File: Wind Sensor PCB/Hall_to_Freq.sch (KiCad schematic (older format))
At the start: 13 parts

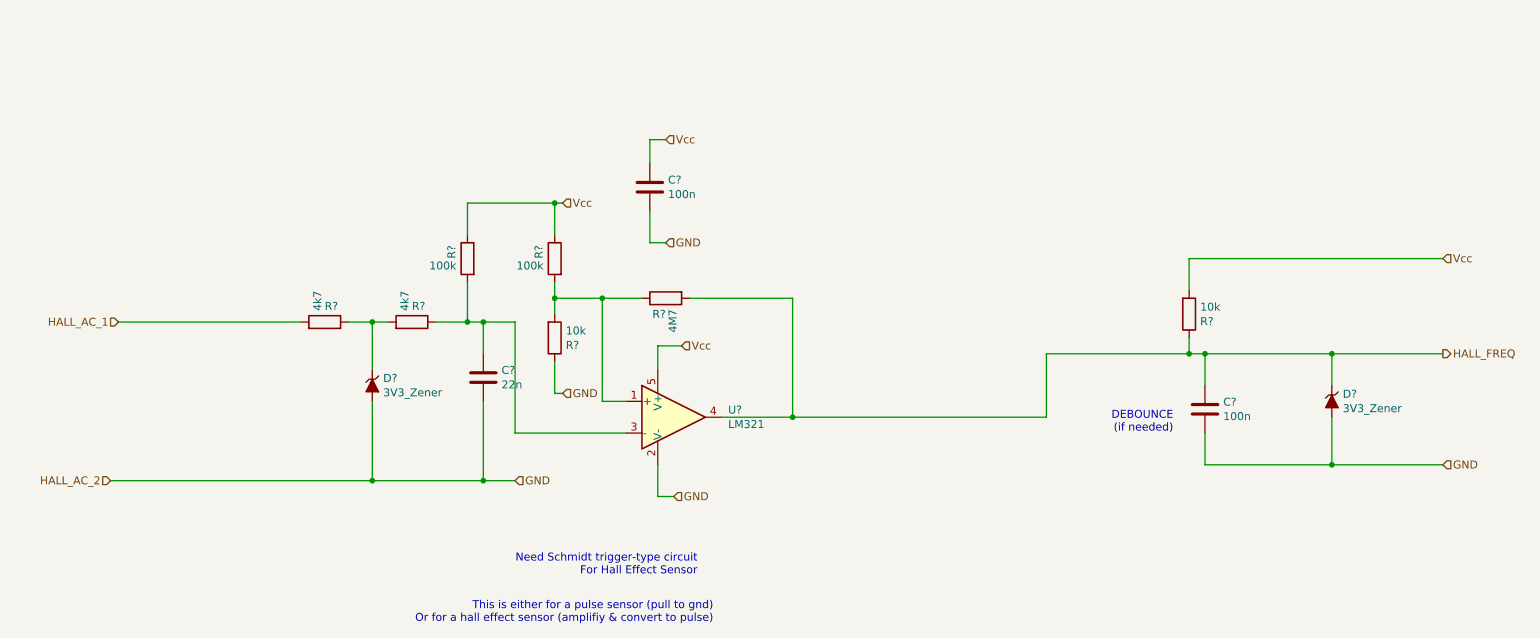
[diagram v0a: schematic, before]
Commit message: Updated PCB
Version 1 of the PCB with ATMEGA328 used...
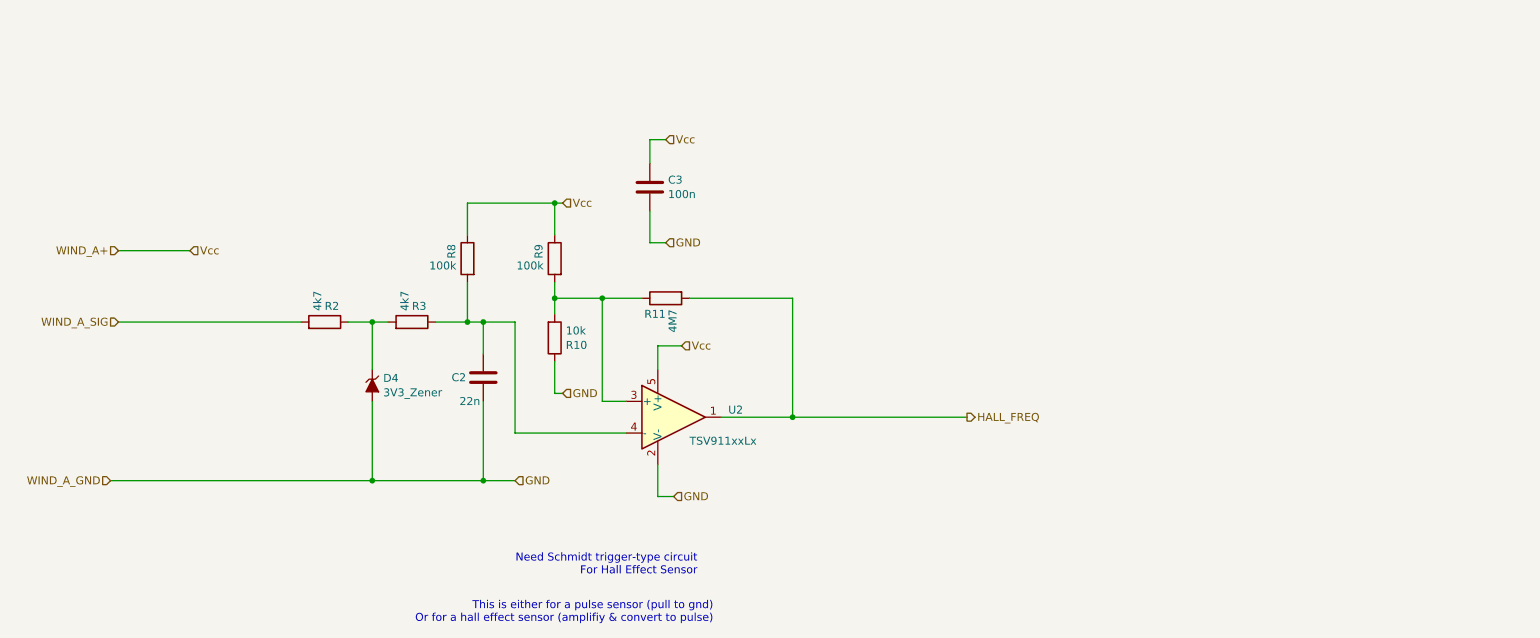
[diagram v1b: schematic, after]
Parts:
- removed C?: 100n, symbol device:C
- removed D?: 3V3_Zener, symbol matts_components:ZENERsmall
- removed R26: 10k, REInnovationFootprint:SM0805, symbol Device:R
- removed U?: LM321, REInnovationFootprint:SM_SOT-23-5, symbol Amplifier_Operational:LM321
- added U2: TSV911xxLx, REInnovationFootprint:SM_SOT-23-5, symbol Amplifier_Operational:TSV911xxLx
- C2, C3: renamed from C?; footprint (none) -> REInnovationFootprint:SM_C_0805
- D4: renamed from D?; footprint (none) -> REInnovationFootprint:SOT23
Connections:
- net GND: now also U2.2 (V-)
- net HALL_FREQ: now also U2.1
- net Vcc: now also U2.5 (V+)
- net at C2.1, R25.1, R35.2: now also U2.4 (-)
- net at R36.2, R37.2, R38.1: now also U2.3 (+)
- net HALL_AC_1 renamed WIND_A_SIG
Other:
- note removed: "DEBOUNCE\n(if needed)\n"
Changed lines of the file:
@@
 $Descr A4 11693 8268
 encoding utf-8
-Sheet 6 6
+Sheet 4 4
 Title ""
 Date ""
@@
 Comment4 ""
 $EndDescr
-Wire Wire Line
-	8300 3500 8300 3600
-Text Notes 8200 4100 2    50   ~ 0
-DEBOUNCE\n(if needed)\n
-Wire Wire Line
-	9200 3800 9200 3600
-Connection ~ 9200 3600
-Wire Wire Line
-	9200 3600 8400 3600
-$Comp
-L Device:R R?
-U 1 1 60751298
-P 8300 3350
-AR Path="/60751298" Ref="R?"  Part="1"
-AR Path="/6073E175/60751298" Ref="R26"  Part="1"
-AR Path="/60F57495/60751298" Ref="R?"  Part="1"
-F 0 "R?" H 8370 3396 50  0000 L CNN
-F 1 "10k" H 8370 3305 50  0000 L CNN
-F 2 "REInnovationFootprint:SM0805" V 8230 3350 50  0001 C CNN
-F 3 "~" H 8300 3350 50  0001 C CNN
-F 4 "Farnell" H 8300 3350 50  0001 C CNN "Supplier 1"
-F 5 "2073607" H 8300 3350 50  0001 C CNN "Supplier 1 Code"
-F 6 "https://uk.farnell.com/multicomp/mcmr08x1002ftl/res-10k-1-0-125w-0805-ceramic/dp/2073607?st=0805%20resistor%2010k" H 8300 3350 50  0001 C CNN "Supplier 1 Web"
-F 7 "0.02" H 8300 3350 50  0001 C CNN "Supplier 1 Cost"
-F 8 "MCMR08X1002FTL" H 8300 3350 50  0001 C CNN "Manufacturer Part"
-F 9 "C17414" H 8300 3350 50  0001 C CNN "LCSC"
-F 10 "Y" H 8300 3350 50  0001 C CNN "JLCPCB Add"
-F 11 "0.0029" H 8300 3350 50  0001 C CNN "JLCPCB Cost"
-	1    8300 3350
-	1    0    0    1
-$EndComp
-Wire Wire Line
-	9200 4300 8400 4300
-Text HLabel 9900 3000 2    50   Input ~ 0
-Vcc
-Text HLabel 9900 3600 2    50   Output ~ 0
+Text HLabel 6900 4000 2    50   Output ~ 0
 HALL_FREQ
-Text HLabel 9900 4300 2    50   Input ~ 0
-GND
-Text HLabel 1550 3400 0    50   Input ~ 0
-HALL_AC_1
-Text HLabel 1500 4400 0    50   Input ~ 0
-HALL_AC_2
 Text Notes 5200 5000 2    50   ~ 0
 Need Schmidt trigger-type circuit\nFor Hall Effect Sensor\n
-Wire Wire Line
-	9200 3600 9900 3600
-Wire Wire Line
-	8300 3000 9900 3000
-Wire Wire Line
-	8300 3000 8300 3200
-Wire Wire Line
-	9900 4300 9200 4300
-Connection ~ 9200 4300
-Wire Wire Line
-	8400 3600 8400 3800
-Connection ~ 8400 3600
-Wire Wire Line
-	8400 3600 8300 3600
-$Comp
-L Amplifier_Operational:LM321 U?
-U 1 1 609A25E3
-P 5050 4000
-F 0 "U?" H 5394 4046 50  0000 L CNN
-F 1 "LM321" H 5394 3955 50  0000 L CNN
-F 2 "REInnovationFootprint:SM_SOT-23-5" H 5050 4000 50  0001 C CNN
-F 3 "http://www.ti.com/lit/ds/symlink/lm321.pdf" H 5050 4000 50  0001 C CNN
-F 4 "Unisonic Tech" H 5050 4000 50  0001 C CNN "Manufacturer"
-F 5 "LM321G-AE5-R" H 5050 4000 50  0001 C CNN "Manufacturer Part"
-F 6 "C100068" H 5050 4000 50  0001 C CNN "LCSC"
-F 7 "Y" H 5050 4000 50  0001 C CNN "JLCPCB Add"
-F 8 "0.0778" H 5050 4000 50  0001 C CNN "JLCPCB Cost"
-	1    5050 4000
-	1    0    0    -1
-$EndComp
 Text HLabel 5100 3550 2    50   Input ~ 0
 Vcc
@@
 AR Path="/607446F0" Ref="R?"  Part="1"
 AR Path="/6073E175/607446F0" Ref="R25"  Part="1"
-AR Path="/60F57495/607446F0" Ref="R?"  Part="1"
-F 0 "R?" V 3500 3400 50  0000 L CNN
+AR Path="/60F57495/607446F0" Ref="R3"  Part="1"
+F 0 "R3" V 3500 3400 50  0000 L CNN
 F 1 "4k7" H 3470 3355 50  0000 L CNN
 F 2 "REInnovationFootprint:SM0805" V 3330 3400 50  0001 C CNN
@@
 AR Path="/607455DE" Ref="R?"  Part="1"
 AR Path="/6073E175/607455DE" Ref="R36"  Part="1"
-AR Path="/60F57495/607455DE" Ref="R?"  Part="1"
-F 0 "R?" V 4400 3000 50  0000 L CNN
+AR Path="/60F57495/607455DE" Ref="R9"  Part="1"
+F 0 "R9" V 4400 3000 50  0000 L CNN
 F 1 "100k" H 4370 2955 50  0000 L CNN
 F 2 "REInnovationFootprint:SM0805" V 4230 3000 50  0001 C CNN
@@
 AR Path="/60748ED5" Ref="R?"  Part="1"
 AR Path="/6073E175/60748ED5" Ref="R38"  Part="1"
-AR Path="/60F57495/60748ED5" Ref="R?"  Part="1"
-F 0 "R?" V 5100 3250 50  0000 L CNN
+AR Path="/60F57495/60748ED5" Ref="R11"  Part="1"
+F 0 "R11" V 5100 3250 50  0000 L CNN
 F 1 "4M7" H 5070 3205 50  0000 L CNN
 F 2 "REInnovationFootprint:SM0805" V 4930 3250 50  0001 C CNN
@@
 Wire Wire Line
 	5800 3250 5800 4000
-Connection ~ 5800 4000
-Wire Wire Line
-	5800 4000 7400 4000
 Wire Wire Line
 	4300 3150 4300 3250
@@
 Wire Wire Line
 	3750 3400 3850 3400
-Wire Wire Line
-	8300 3600 7400 3600
-Wire Wire Line
-	7400 3600 7400 4000
-Connection ~ 8300 3600
 Wire Wire Line
 	4050 4400 3850 4400
@@
 AR Path="/6079CF2E" Ref="R?"  Part="1"
 AR Path="/6073E175/6079CF2E" Ref="R37"  Part="1"
-AR Path="/60F57495/6079CF2E" Ref="R?"  Part="1"
-F 0 "R?" H 4370 3546 50  0000 L CNN
+AR Path="/60F57495/6079CF2E" Ref="R10"  Part="1"
+F 0 "R10" H 4370 3546 50  0000 L CNN
 F 1 "10k" H 4370 3455 50  0000 L CNN
 F 2 "REInnovationFootprint:SM0805" V 4230 3500 50  0001 C CNN
@@
 AR Path="/6079D863" Ref="R?"  Part="1"
 AR Path="/6073E175/6079D863" Ref="R35"  Part="1"
-AR Path="/60F57495/6079D863" Ref="R?"  Part="1"
-F 0 "R?" V 3850 3000 50  0000 L CNN
+AR Path="/60F57495/6079D863" Ref="R8"  Part="1"
+F 0 "R8" V 3850 3000 50  0000 L CNN
 F 1 "100k" H 3820 2955 50  0000 L CNN
 F 2 "REInnovationFootprint:SM0805" V 3680 3000 50  0001 C CNN
@@
 AR Path="/6079E09B" Ref="R?"  Part="1"
 AR Path="/6073E175/6079E09B" Ref="R24"  Part="1"
-AR Path="/60F57495/6079E09B" Ref="R?"  Part="1"
-F 0 "R?" V 2950 3400 50  0000 L CNN
+AR Path="/60F57495/6079E09B" Ref="R2"  Part="1"
+F 0 "R2" V 2950 3400 50  0000 L CNN
 F 1 "4k7" H 2920 3355 50  0000 L CNN
 F 2 "REInnovationFootprint:SM0805" V 2780 3400 50  0001 C CNN
@@
 $EndComp
 Wire Wire Line
-	1550 3400 2700 3400
-Wire Wire Line
 	1500 4400 3150 4400
 $Comp
-L matts_components:ZENERsmall D?
-U 1 1 60F5F219
-P 9200 3900
-F 0 "D?" V 9154 3969 50  0000 L CNN
-F 1 "3V3_Zener" V 9245 3969 50  0000 L CNN
-F 2 "" H 9200 3900 50  0000 C CNN
-F 3 "" H 9200 3900 50  0000 C CNN
-	1    9200 3900
-	0    1    1    0
-$EndComp
-$Comp
-L matts_components:ZENERsmall D?
+L matts_components:ZENERsmall D4
 U 1 1 60F5F616
 P 3150 3800
-F 0 "D?" V 3104 3869 50  0000 L CNN
+F 0 "D4" V 3104 3869 50  0000 L CNN
 F 1 "3V3_Zener" V 3195 3869 50  0000 L CNN
-F 2 "" H 3150 3800 50  0000 C CNN
+F 2 "REInnovationFootprint:SOT23" H 3150 3800 50  0001 C CNN
 F 3 "" H 3150 3800 50  0000 C CNN
 	1    3150 3800
@@
 $EndComp
 $Comp
-L device:C C?
-U 1 1 60F5FBE8
-P 8400 3950
-F 0 "C?" H 8515 3996 50  0000 L CNN
-F 1 "100n" H 8515 3905 50  0000 L CNN
-F 2 "" H 8438 3800 50  0001 C CNN
-F 3 "~" H 8400 3950 50  0001 C CNN
-	1    8400 3950
-	1    0    0    -1
-$EndComp
-$Comp
-L device:C C?
+L device:C C3
 U 1 1 60F5FEAC
 P 4900 2550
-F 0 "C?" H 5015 2596 50  0000 L CNN
+F 0 "C3" H 5015 2596 50  0000 L CNN
 F 1 "100n" H 5015 2505 50  0000 L CNN
-F 2 "" H 4938 2400 50  0001 C CNN
+F 2 "REInnovationFootprint:SM_C_0805" H 4938 2400 50  0001 C CNN
 F 3 "~" H 4900 2550 50  0001 C CNN
 	1    4900 2550
@@
 $EndComp
 $Comp
-L device:C C?
+L device:C C2
 U 1 1 60F601A3
 P 3850 3750
-F 0 "C?" H 3965 3796 50  0000 L CNN
-F 1 "22n" H 3965 3705 50  0000 L CNN
-F 2 "" H 3888 3600 50  0001 C CNN
+F 0 "C2" H 3650 3750 50  0000 L CNN
+F 1 "22n" H 3700 3600 50  0000 L CNN
+F 2 "REInnovationFootprint:SM_C_0805" H 3888 3600 50  0001 C CNN
 F 3 "~" H 3850 3750 50  0001 C CNN
 	1    3850 3750
@@
 Wire Wire Line
 	3150 3400 3150 3700
-Wire Wire Line
-	8400 4100 8400 4300
-Wire Wire Line
-	9200 4000 9200 4300
+$Comp
+L Amplifier_Operational:TSV911xxLx U?
+U 1 1 60F5D203
+P 5050 4000
+AR Path="/60F5D203" Ref="U?"  Part="1"
+AR Path="/60F87947/60F5D203" Ref="U?"  Part="1"
+AR Path="/60F57495/60F5D203" Ref="U2"  Part="1"
+F 0 "U2" H 5394 4046 50  0000 L CNN
+F 1 "TSV911xxLx" H 5150 3850 50  0000 L CNN
+F 2 "REInnovationFootprint:SM_SOT-23-5" H 4950 3800 50  0001 L CNN
+F 3 "www.st.com/resource/en/datasheet/tsv911.pdf" H 5050 4200 50  0001 C CNN
+F 4 "C361052" H 5050 4000 50  0001 C CNN "LCSC"
+F 5 "Y" H 5050 4000 50  0001 C CNN "JLCPCB Add"
+F 6 "0.4576" H 5050 4000 50  0001 C CNN "JLCPCB Cost"
+	1    5050 4000
+	1    0    0    -1
+$EndComp
+Text HLabel 1550 2950 0    50   Input ~ 0
+WIND_A+
+Text HLabel 1500 4400 0    50   Input ~ 0
+WIND_A_GND
+Text HLabel 1550 3400 0    50   Input ~ 0
+WIND_A_SIG
+Wire Wire Line
+	1550 2950 2000 2950
+Wire Wire Line
+	1550 3400 2700 3400
+Text HLabel 2000 2950 2    50   Input ~ 0
+Vcc
+Wire Wire Line
+	5800 4000 6900 4000
+Connection ~ 5800 4000
 $EndSCHEMATC

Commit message: large code update
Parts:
- removed R38: 4M7, REInnovationFootprint:SM0805, symbol Device:R
- C2: JLCPCB Add (none) -> Y; LCSC (none) -> C1804
- D4: footprint REInnovationFootprint:SOT23 -> REInnovationFootprint:SOT23_ZENER; JLCPCB Add (none) -> Y; LCSC (none) -> C130247
- R35: value 100k -> 470k; JLCPCB Cost 0.0034 -> (none); LCSC C17407 -> (none); Manufacturer Part MCWR08X1001FTL -> (none)
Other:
- note added: "Hall effect - between Gnd and SIG\nPulse between +v and SIG\nThis will work for both"
- note added: "OLD Switching Thresholds:\nRtu = (4M7*100k) / (4M7+100k)\nRtu = 97.9k\nVusl = 3.3*10k/(97.9k +10k) = 0.1667V\n\nRtl = (10k*4M7)/(10k+4M7) = 9.97k\nVlsl = 3.3 * 9.97k /(100k+9.97k) = 0.299V\n\nThis will always be on?\nAs lower level is higher than upper level. Never switches off."
- note added: "ORIGINAL"
- note added: "Switching Thresholds:\nRtu = (10k*100k) / (10k +100k)\nRtu = 9.09k\nVusl = 3.3*10k/(9.09k +10k) = 1.7828V\n\nRtl = (10k*10k)/(10k+10k) = 5k\nVlsl = 3.3 * 5k /(100k+5k) = 0.157V\n\n"
- note added: "UPDATED"
- moved on the sheet: C2, C3, D4, R10, R2, R3, R8, R9, U2
